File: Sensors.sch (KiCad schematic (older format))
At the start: 6 parts, among them U300 BMP280, U301 BMI088

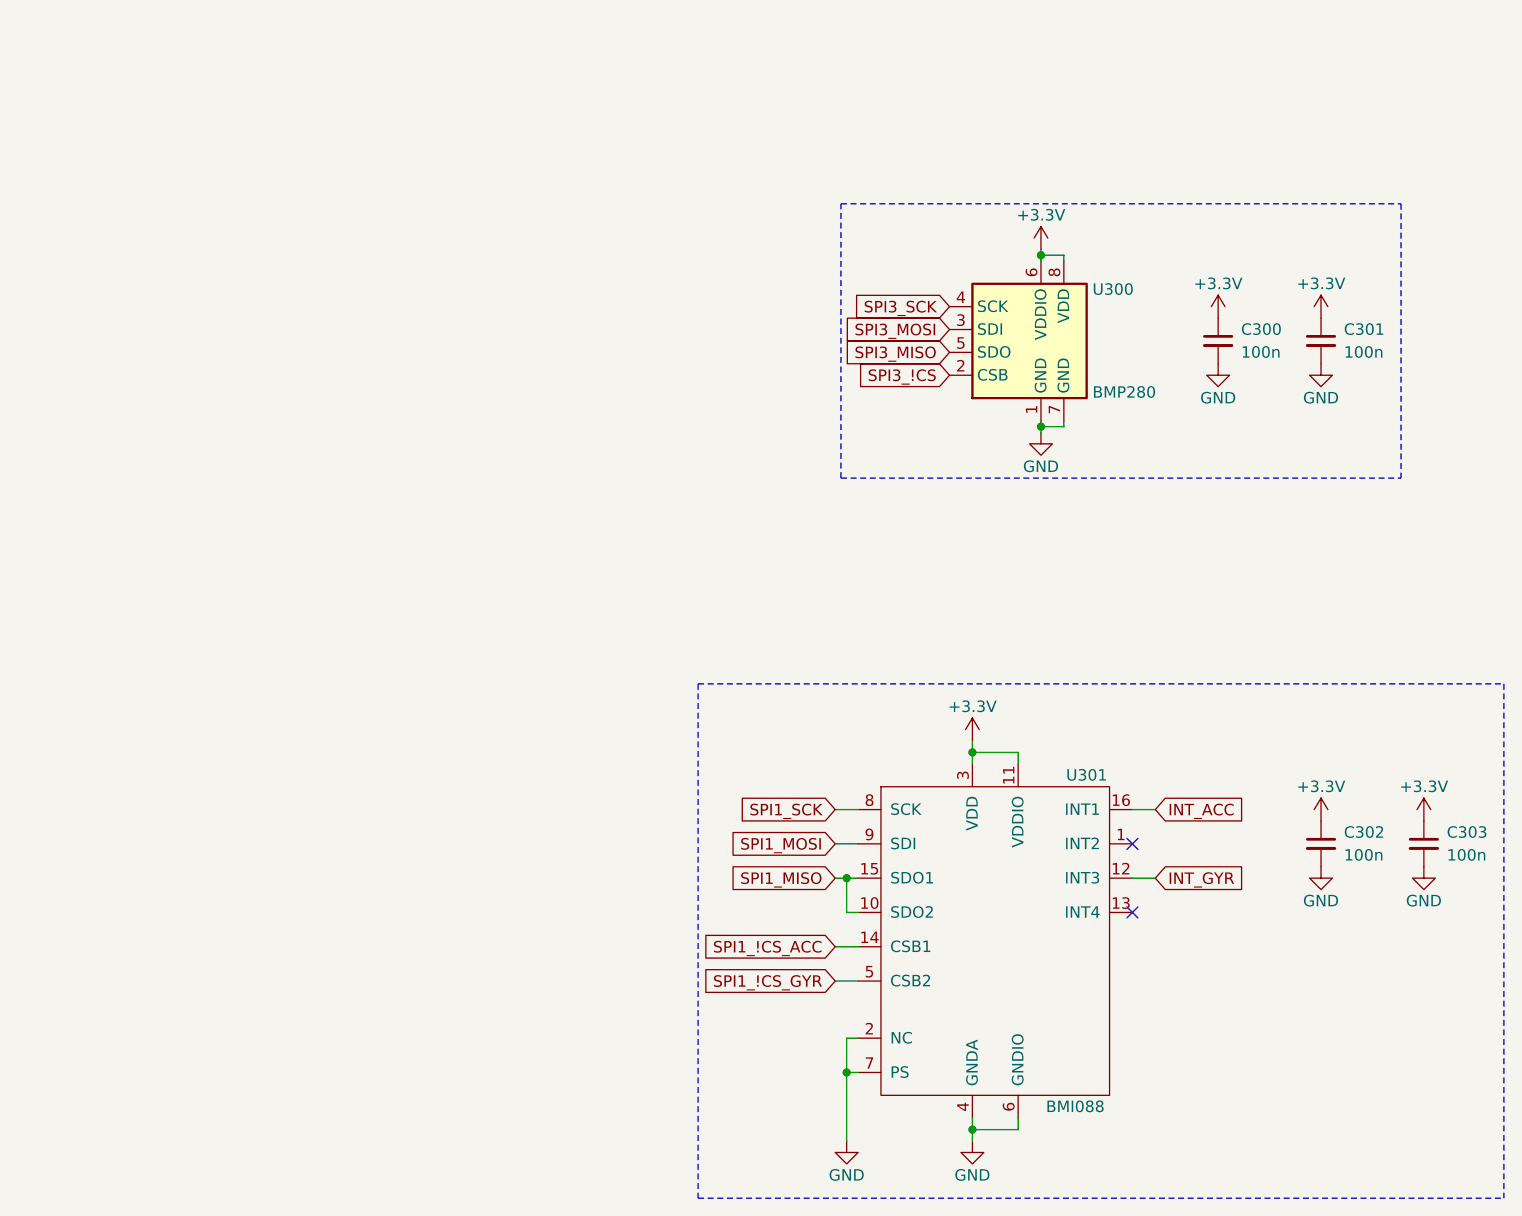
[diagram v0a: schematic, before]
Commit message: Updated firmware. Added schematic PDF.
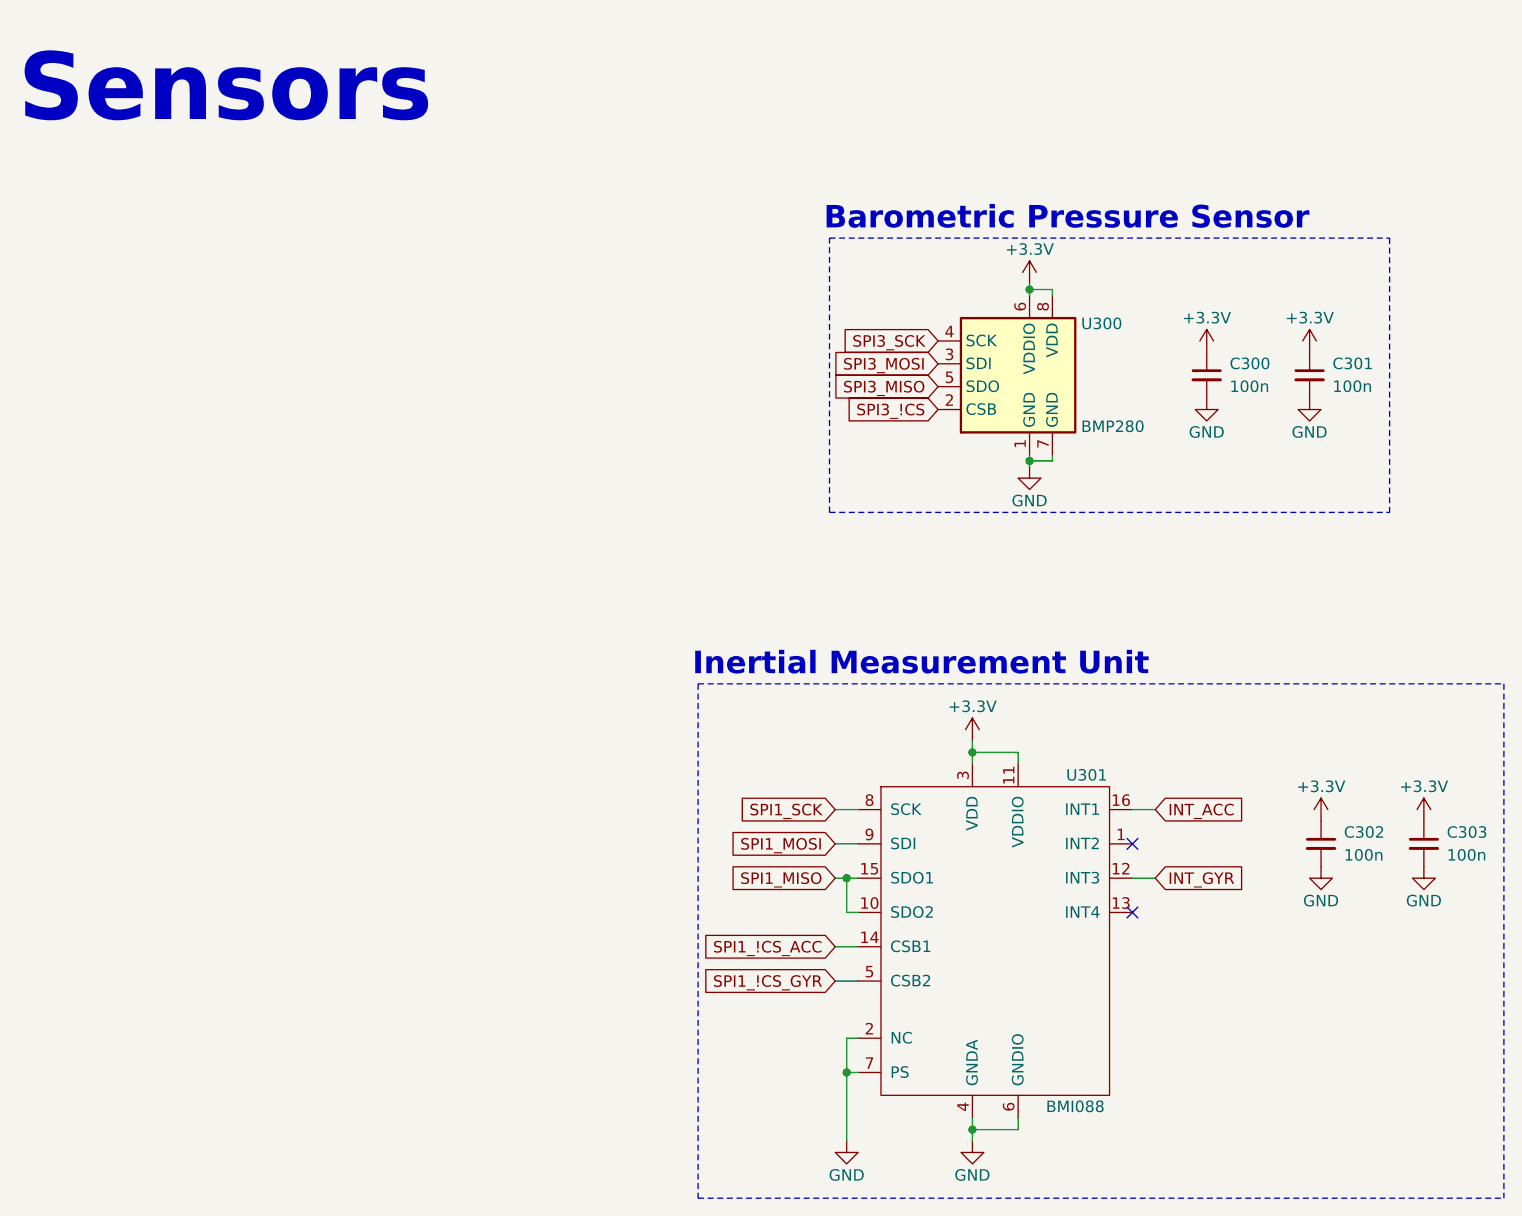
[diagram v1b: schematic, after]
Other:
- note added: "Barometric Pressure Sensor"
- note added: "Inertial Measurement Unit"
- note added: "Sensors"
- moved on the sheet: C300, C301, U300
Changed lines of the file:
@@
 L Sensor_Pressure:BMP280 U?
 U 1 1 5F8494F2
-P 5400 2250
+P 5350 2400
 AR Path="/5F8494F2" Ref="U?"  Part="1"
 AR Path="/5F83C004/5F8494F2" Ref="U300"  Part="1"
-F 0 "U300" H 5625 2525 50  0000 L CNN
-F 1 "BMP280" H 5625 2075 50  0000 L CNN
-F 2 "Package_LGA:Bosch_LGA-8_2x2.5mm_P0.65mm_ClockwisePinNumbering" H 5400 1550 50  0001 C CNN
-F 3 "https://ae-bst.resource.bosch.com/media/_tech/media/datasheets/BST-BMP280-DS001.pdf" H 5400 2250 50  0001 C CNN
-F 4 "C233787" H 5400 2250 50  0001 C CNN "LCSC Part #"
-	1    5400 2250
-	1    0    0    -1
-$EndComp
-Text GLabel 5000 2350 0    50   Input ~ 0
+F 0 "U300" H 5575 2675 50  0000 L CNN
+F 1 "BMP280" H 5575 2225 50  0000 L CNN
+F 2 "Package_LGA:Bosch_LGA-8_2x2.5mm_P0.65mm_ClockwisePinNumbering" H 5350 1700 50  0001 C CNN
+F 3 "https://ae-bst.resource.bosch.com/media/_tech/media/datasheets/BST-BMP280-DS001.pdf" H 5350 2400 50  0001 C CNN
+F 4 "C233787" H 5350 2400 50  0001 C CNN "LCSC Part #"
+	1    5350 2400
+	1    0    0    -1
+$EndComp
+Text GLabel 4950 2500 0    50   Input ~ 0
 SPI3_!CS
-Text GLabel 5000 2150 0    50   Input ~ 0
+Text GLabel 4950 2300 0    50   Input ~ 0
 SPI3_MOSI
-Text GLabel 5000 2250 0    50   Input ~ 0
+Text GLabel 4950 2400 0    50   Input ~ 0
 SPI3_MISO
-Text GLabel 5000 2050 0    50   Input ~ 0
+Text GLabel 4950 2200 0    50   Input ~ 0
 SPI3_SCK
 $Comp
 L power:GND #PWR?
 U 1 1 5F8494FC
-P 5400 2600
+P 5350 2750
 AR Path="/5F8494FC" Ref="#PWR?"  Part="1"
 AR Path="/5F83C004/5F8494FC" Ref="#PWR042"  Part="1"
-F 0 "#PWR042" H 5400 2350 50  0001 C CNN
-F 1 "GND" H 5400 2450 50  0000 C CNN
-F 2 "" H 5400 2600 50  0001 C CNN
-F 3 "" H 5400 2600 50  0001 C CNN
-	1    5400 2600
-	1    0    0    -1
-$EndComp
-Wire Wire Line
-	5400 2600 5400 2575
-Wire Wire Line
-	5400 2575 5500 2575
-Wire Wire Line
-	5500 2575 5500 2550
-Connection ~ 5400 2575
-Wire Wire Line
-	5400 2575 5400 2550
+F 0 "#PWR042" H 5350 2500 50  0001 C CNN
+F 1 "GND" H 5350 2600 50  0000 C CNN
+F 2 "" H 5350 2750 50  0001 C CNN
+F 3 "" H 5350 2750 50  0001 C CNN
+	1    5350 2750
+	1    0    0    -1
+$EndComp
+Wire Wire Line
+	5350 2750 5350 2725
+Wire Wire Line
+	5350 2725 5450 2725
+Wire Wire Line
+	5450 2725 5450 2700
+Connection ~ 5350 2725
+Wire Wire Line
+	5350 2725 5350 2700
 $Comp
 L power:+3.3V #PWR?
 U 1 1 5F849507
-P 5400 1800
+P 5350 1950
 AR Path="/5F849507" Ref="#PWR?"  Part="1"
 AR Path="/5F83C004/5F849507" Ref="#PWR041"  Part="1"
-F 0 "#PWR041" H 5400 1650 50  0001 C CNN
-F 1 "+3.3V" H 5400 1950 50  0000 C CNN
-F 2 "" H 5400 1800 50  0001 C CNN
-F 3 "" H 5400 1800 50  0001 C CNN
-	1    5400 1800
-	1    0    0    -1
-$EndComp
-Wire Wire Line
-	5400 1800 5400 1825
-Wire Wire Line
-	5400 1825 5500 1825
-Wire Wire Line
-	5500 1825 5500 1850
-Connection ~ 5400 1825
-Wire Wire Line
-	5400 1825 5400 1850
+F 0 "#PWR041" H 5350 1800 50  0001 C CNN
+F 1 "+3.3V" H 5350 2100 50  0000 C CNN
+F 2 "" H 5350 1950 50  0001 C CNN
+F 3 "" H 5350 1950 50  0001 C CNN
+	1    5350 1950
+	1    0    0    -1
+$EndComp
+Wire Wire Line
+	5350 1950 5350 1975
+Wire Wire Line
+	5350 1975 5450 1975
+Wire Wire Line
+	5450 1975 5450 2000
+Connection ~ 5350 1975
+Wire Wire Line
+	5350 1975 5350 2000
 $Comp
 L Device:C_Small C?
 U 1 1 5F849512
-P 6175 2200
+P 6125 2350
 AR Path="/5F849512" Ref="C?"  Part="1"
 AR Path="/5F83C004/5F849512" Ref="C300"  Part="1"
-F 0 "C300" H 6275 2250 50  0000 L CNN
-F 1 "100n" H 6275 2150 50  0000 L CNN
-F 2 "Capacitor_SMD:C_0402_1005Metric" H 6175 2200 50  0001 C CNN
-F 3 "~" H 6175 2200 50  0001 C CNN
-F 4 "C1525" H 6175 2200 50  0001 C CNN "LCSC Part #"
-	1    6175 2200
+F 0 "C300" H 6225 2400 50  0000 L CNN
+F 1 "100n" H 6225 2300 50  0000 L CNN
+F 2 "Capacitor_SMD:C_0402_1005Metric" H 6125 2350 50  0001 C CNN
+F 3 "~" H 6125 2350 50  0001 C CNN
+F 4 "C1525" H 6125 2350 50  0001 C CNN "LCSC Part #"
+	1    6125 2350
 	1    0    0    -1
 $EndComp
@@
 L power:+3.3V #PWR?
 U 1 1 5F849518
-P 6175 2100
+P 6125 2250
 AR Path="/5F849518" Ref="#PWR?"  Part="1"
 AR Path="/5F83C004/5F849518" Ref="#PWR043"  Part="1"
-F 0 "#PWR043" H 6175 1950 50  0001 C CNN
-F 1 "+3.3V" H 6175 2250 50  0000 C CNN
-F 2 "" H 6175 2100 50  0001 C CNN
-F 3 "" H 6175 2100 50  0001 C CNN
-	1    6175 2100
+F 0 "#PWR043" H 6125 2100 50  0001 C CNN
+F 1 "+3.3V" H 6125 2400 50  0000 C CNN
+F 2 "" H 6125 2250 50  0001 C CNN
+F 3 "" H 6125 2250 50  0001 C CNN
+	1    6125 2250
 	1    0    0    -1
 $EndComp
@@
 L power:GND #PWR?
 U 1 1 5F84951E
-P 6175 2300
+P 6125 2450
 AR Path="/5F84951E" Ref="#PWR?"  Part="1"
 AR Path="/5F83C004/5F84951E" Ref="#PWR044"  Part="1"
-F 0 "#PWR044" H 6175 2050 50  0001 C CNN
-F 1 "GND" H 6175 2150 50  0000 C CNN
-F 2 "" H 6175 2300 50  0001 C CNN
-F 3 "" H 6175 2300 50  0001 C CNN
-	1    6175 2300
+F 0 "#PWR044" H 6125 2200 50  0001 C CNN
+F 1 "GND" H 6125 2300 50  0000 C CNN
+F 2 "" H 6125 2450 50  0001 C CNN
+F 3 "" H 6125 2450 50  0001 C CNN
+	1    6125 2450
 	1    0    0    -1
 $EndComp
@@
 L Device:C_Small C?
 U 1 1 5F849524
-P 6625 2200
+P 6575 2350
 AR Path="/5F849524" Ref="C?"  Part="1"
 AR Path="/5F83C004/5F849524" Ref="C301"  Part="1"
-F 0 "C301" H 6725 2250 50  0000 L CNN
-F 1 "100n" H 6725 2150 50  0000 L CNN
-F 2 "Capacitor_SMD:C_0402_1005Metric" H 6625 2200 50  0001 C CNN
-F 3 "~" H 6625 2200 50  0001 C CNN
-F 4 "C1525" H 6625 2200 50  0001 C CNN "LCSC Part #"
-	1    6625 2200
+F 0 "C301" H 6675 2400 50  0000 L CNN
+F 1 "100n" H 6675 2300 50  0000 L CNN
+F 2 "Capacitor_SMD:C_0402_1005Metric" H 6575 2350 50  0001 C CNN
+F 3 "~" H 6575 2350 50  0001 C CNN
+F 4 "C1525" H 6575 2350 50  0001 C CNN "LCSC Part #"
+	1    6575 2350
 	1    0    0    -1
 $EndComp
@@
 L power:+3.3V #PWR?
 U 1 1 5F84952A
-P 6625 2100
+P 6575 2250
 AR Path="/5F84952A" Ref="#PWR?"  Part="1"
 AR Path="/5F83C004/5F84952A" Ref="#PWR045"  Part="1"
-F 0 "#PWR045" H 6625 1950 50  0001 C CNN
-F 1 "+3.3V" H 6625 2250 50  0000 C CNN
-F 2 "" H 6625 2100 50  0001 C CNN
-F 3 "" H 6625 2100 50  0001 C CNN
-	1    6625 2100
+F 0 "#PWR045" H 6575 2100 50  0001 C CNN
+F 1 "+3.3V" H 6575 2400 50  0000 C CNN
+F 2 "" H 6575 2250 50  0001 C CNN
+F 3 "" H 6575 2250 50  0001 C CNN
+	1    6575 2250
 	1    0    0    -1
 $EndComp
@@
 L power:GND #PWR?
 U 1 1 5F849530
-P 6625 2300
+P 6575 2450
 AR Path="/5F849530" Ref="#PWR?"  Part="1"
 AR Path="/5F83C004/5F849530" Ref="#PWR046"  Part="1"
-F 0 "#PWR046" H 6625 2050 50  0001 C CNN
-F 1 "GND" H 6625 2150 50  0000 C CNN
-F 2 "" H 6625 2300 50  0001 C CNN
-F 3 "" H 6625 2300 50  0001 C CNN
-	1    6625 2300
-	1    0    0    -1
-$EndComp
-Wire Notes Line
-	4525 2800 4525 1600
-Wire Notes Line
-	6975 1600 6975 2800
+F 0 "#PWR046" H 6575 2200 50  0001 C CNN
+F 1 "GND" H 6575 2300 50  0000 C CNN
+F 2 "" H 6575 2450 50  0001 C CNN
+F 3 "" H 6575 2450 50  0001 C CNN
+	1    6575 2450
+	1    0    0    -1
+$EndComp
+Wire Notes Line
+	4475 2950 4475 1750
+Wire Notes Line
+	6925 1750 6925 2950
 Text GLabel 4500 4850 0    50   Input ~ 0
 SPI1_!CS_ACC
@@
 	3900 3700 3900 5950
 Wire Notes Line
-	4525 2800 6975 2800
-Wire Notes Line
-	4525 1600 6975 1600
+	4475 2950 6925 2950
+Wire Notes Line
+	4475 1750 6925 1750
 Wire Notes Line
 	3900 5950 7425 5950
 Wire Notes Line
 	3900 3700 7425 3700
+Text Notes 925  1275 0    295  ~ 59
+Sensors
+Text Notes 4450 1725 0    98   ~ 20
+Barometric Pressure Sensor
+Text Notes 3875 3675 0    98   ~ 20
+Inertial Measurement Unit
 $EndSCHEMATC
